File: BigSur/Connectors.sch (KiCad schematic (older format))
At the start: 32 parts, among them J1 XT30, J10 XT30, J11 Conn_01x03, J12 XT30, J13 Conn_01x04, J14 XT30, J15 XT30, J16 XT30, J2 XT30, J3 XT30, J4 XT30, J5 XT30, J6 XT30, J7 XT30, J8 XT30, J9 XT30, U4 SMD46

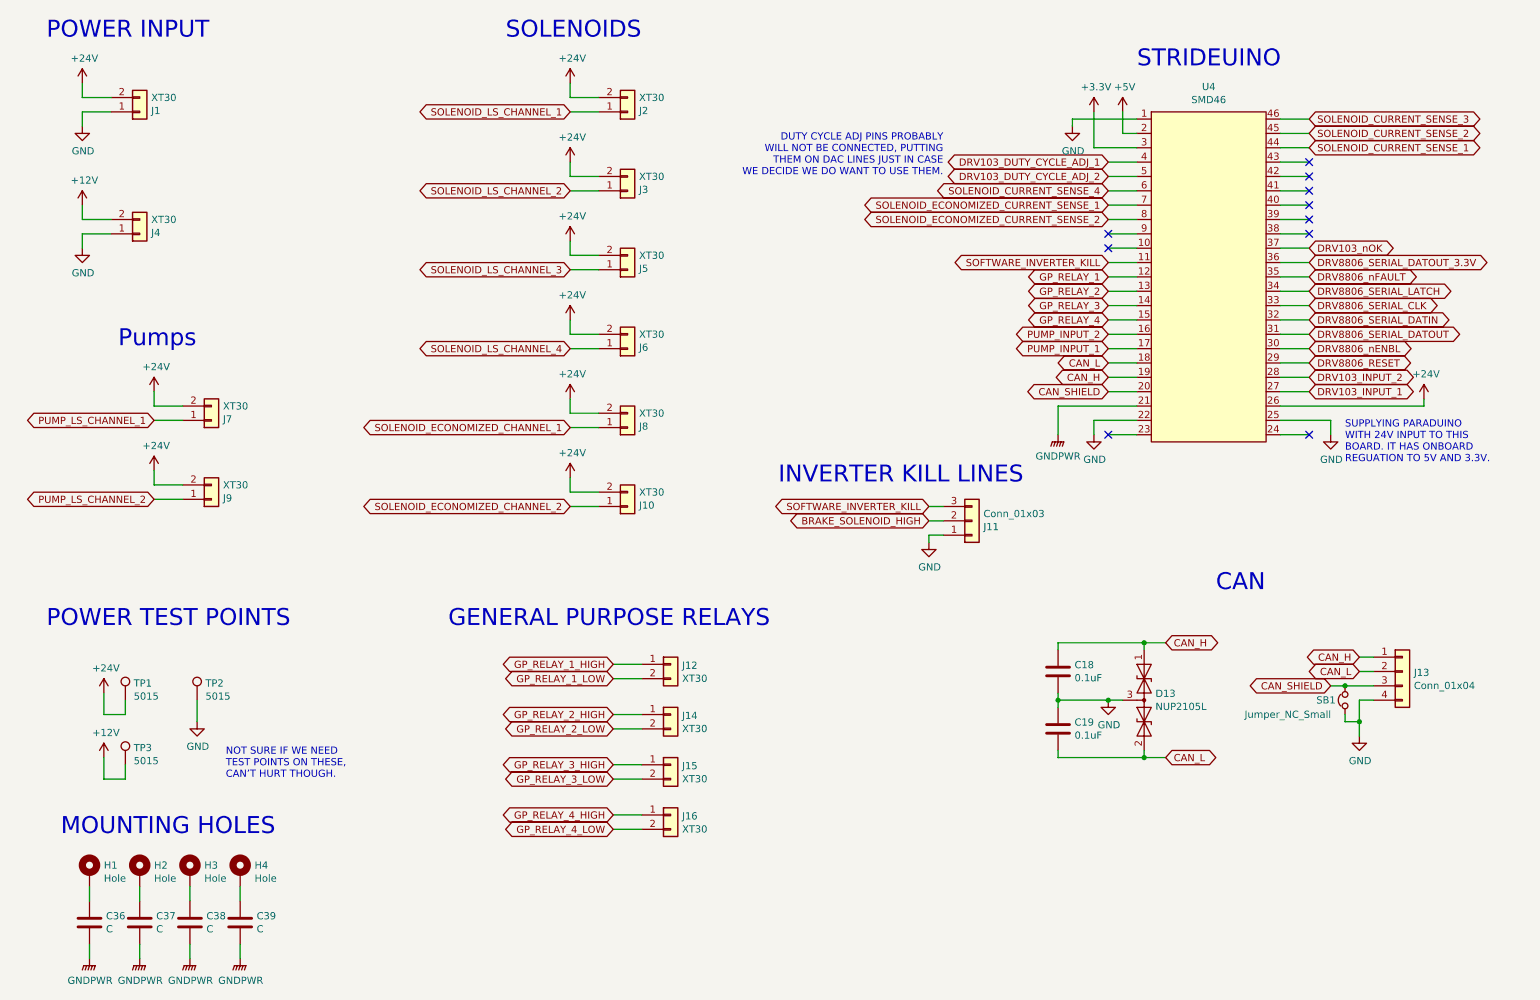
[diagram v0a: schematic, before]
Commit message: XT30 sourcing and footprints
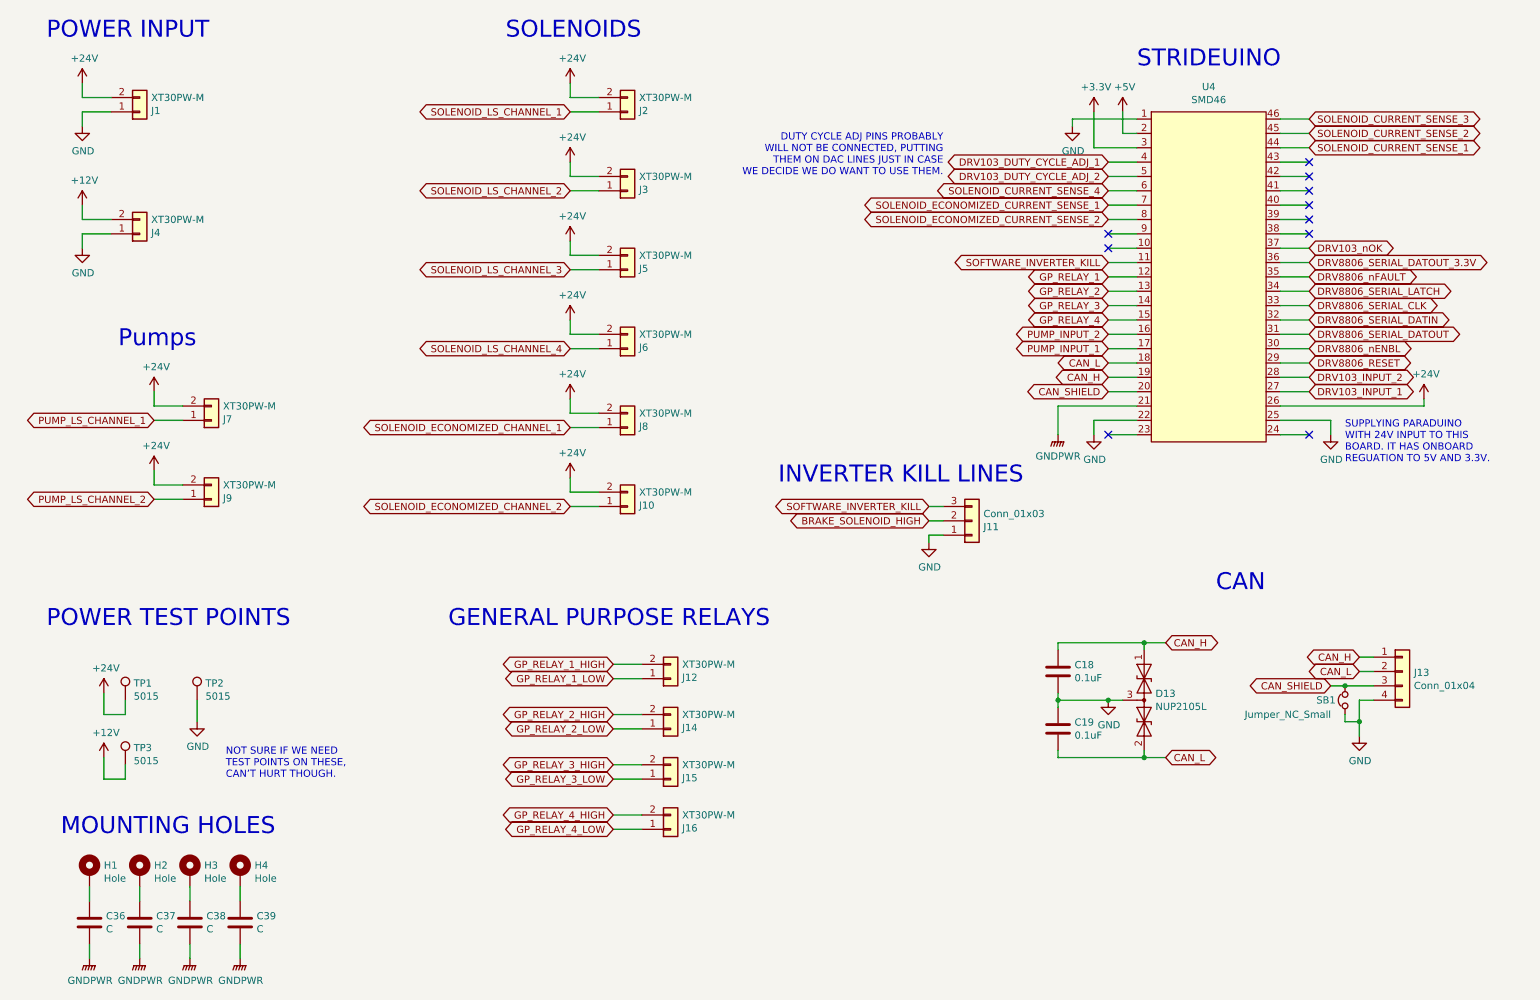
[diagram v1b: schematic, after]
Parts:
- J1, J10, J12, J14, J15, J16, J2, J3, J4, J5, J6, J7, J8, J9: value XT30 -> XT30PW-M; footprint (none) -> BigSur:AMASS_XT30PW-M; AliExpress (none) -> https://www.aliexpress.com/item/32689137918.html
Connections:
- net GP_RELAY_1_HIGH: now also J12.2 (Pin_2); no longer J12.1 (Pin_1)
- net GP_RELAY_1_LOW: now also J12.1 (Pin_1); no longer J12.2 (Pin_2)
- net GP_RELAY_2_HIGH: now also J14.2 (Pin_2); no longer J14.1 (Pin_1)
- net GP_RELAY_2_LOW: now also J14.1 (Pin_1); no longer J14.2 (Pin_2)
- net GP_RELAY_3_HIGH: now also J15.2 (Pin_2); no longer J15.1 (Pin_1)
- net GP_RELAY_3_LOW: now also J15.1 (Pin_1); no longer J15.2 (Pin_2)
- net GP_RELAY_4_HIGH: now also J16.2 (Pin_2); no longer J16.1 (Pin_1)
- net GP_RELAY_4_LOW: now also J16.1 (Pin_1); no longer J16.2 (Pin_2)

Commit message: Switched to active low brake lines
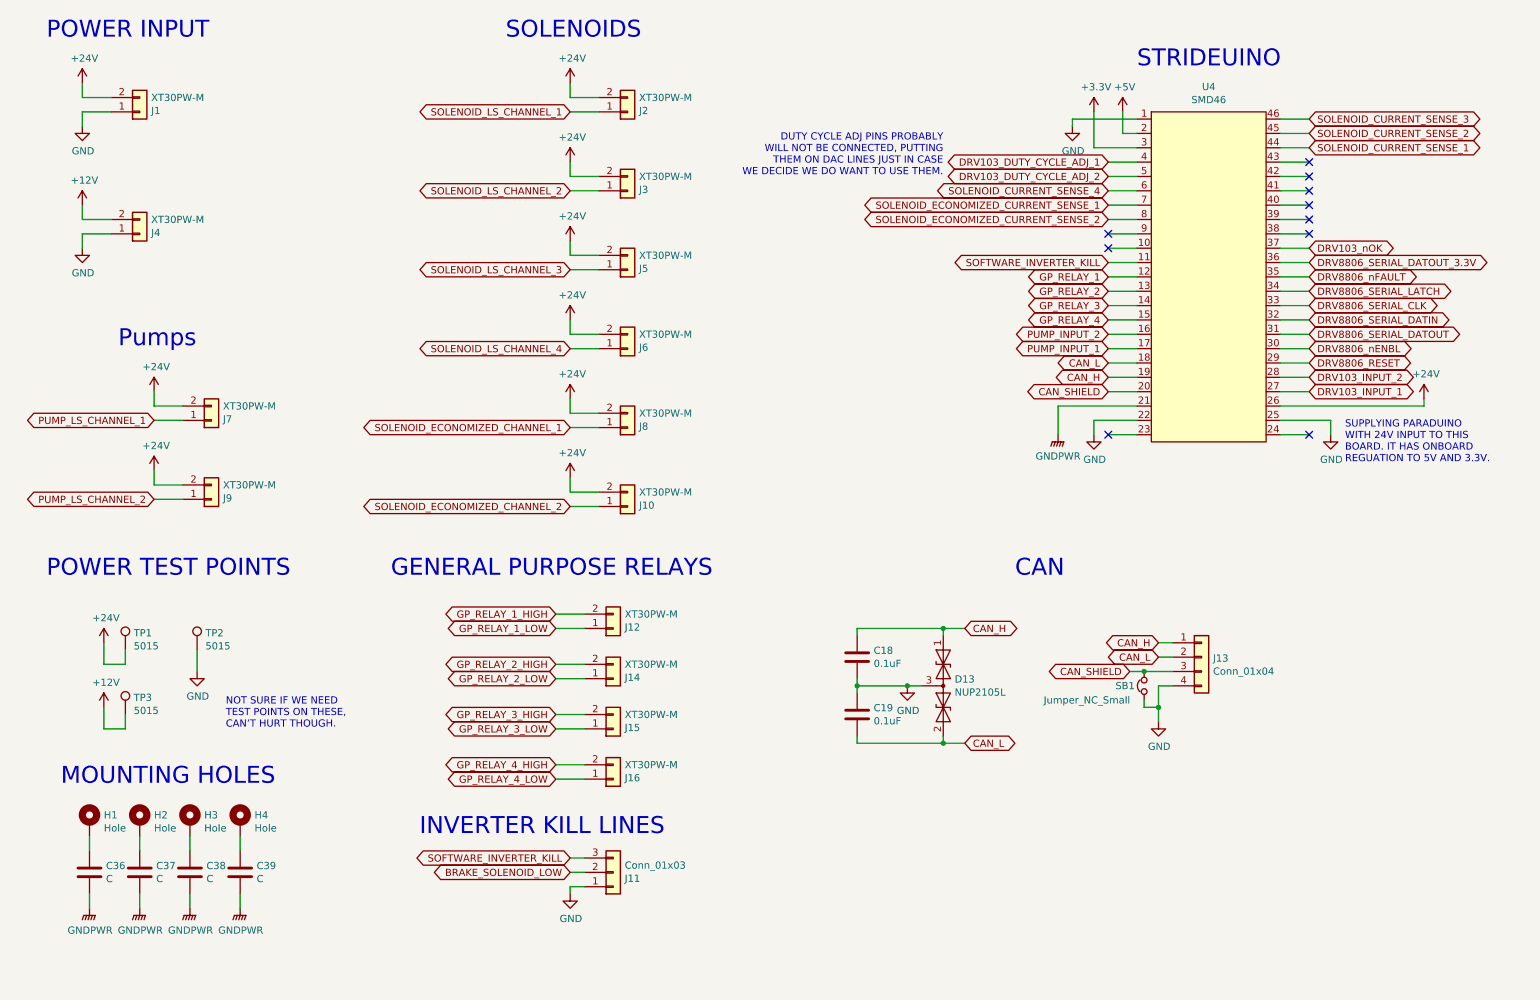
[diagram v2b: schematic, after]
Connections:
- net BRAKE_SOLENOID_HIGH renamed BRAKE_SOLENOID_LOW
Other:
- moved on the sheet: C18, C19, C36, C37, C38, C39, D13, H1, H2, H3, H4, J11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

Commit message: Initial layout pass. This will be changed many times I'm sure.
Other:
- note added: "PUMPS"
- note removed: "Pumps"
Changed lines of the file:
@@
 SOLENOID_ECONOMIZED_CHANNEL_2
 Text Notes 1350 3300 0    118  ~ 0
-Pumps
+PUMPS
 Wire Wire Line
 	1800 3700 1600 3700

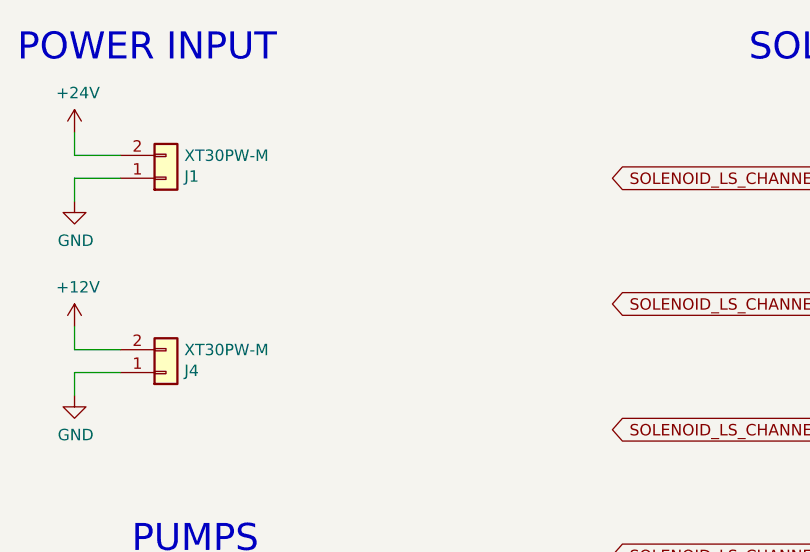
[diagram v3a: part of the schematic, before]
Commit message: Added power LEDs.
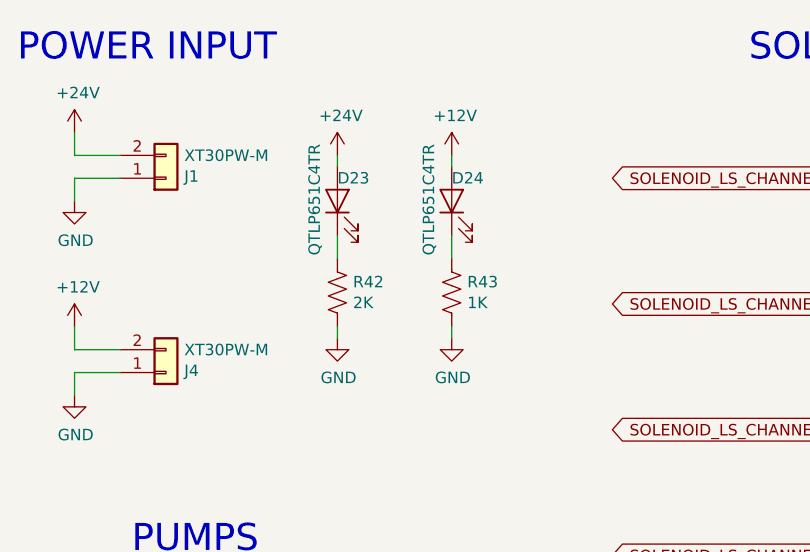
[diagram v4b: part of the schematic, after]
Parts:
- added D23, D24: QTLP651C4TR, LED_SMD:LED_1206_3216Metric_Pad1.42x1.75mm_HandSolder, symbol Device:LED
- added R42: 2K, Resistor_SMD:R_0603_1608Metric_Pad1.05x0.95mm_HandSolder, symbol Device:R_US
- added R43: 1K, Resistor_SMD:R_0603_1608Metric_Pad1.05x0.95mm_HandSolder, symbol Device:R_US
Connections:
- net +12V: now also D24.2 (A)
- net +24V: now also D23.2 (A)
- net GND: now also R42.2, R43.2
- new net: D23.1 (K), R42.1
- new net: D24.1 (K), R43.1
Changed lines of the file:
@@
 	1    0    0    1
 $EndComp
+$Comp
+L Device:LED D?
+U 1 1 5DC6BC2D
+P 2250 1750
+AR Path="/5D6EB2B2/5DC6BC2D" Ref="D?"  Part="1"
+AR Path="/5D71C3EA/5DC6BC2D" Ref="D23"  Part="1"
+F 0 "D23" V 2350 1750 50  0000 R CNN
+F 1 "QTLP651C4TR" H 2500 1850 50  0000 R CNN
+F 2 "LED_SMD:LED_1206_3216Metric_Pad1.42x1.75mm_HandSolder" H 2250 1750 50  0001 C CNN
+F 3 "https://media.digikey.com/pdf/Data%20Sheets/Everlight%20PDFs/QTLP651C-2,3,4,7,B.pdf" H 2250 1750 50  0001 C CNN
+F 4 "https://www.digikey.ca/product-detail/en/everlight-electronics-co-ltd/QTLP651C4TR/1080-1484-1-ND/7598723" V 2250 1750 50  0001 C CNN "Digikey"
+	1    2250 1750
+	0    -1   -1   0
+$EndComp
+$Comp
+L power:+24V #PWR0125
+U 1 1 5DC71029
+P 2250 1550
+AR Path="/5D71C3EA/5DC71029" Ref="#PWR0125"  Part="1"
+AR Path="/5D7D29A6/5DC71029" Ref="#PWR?"  Part="1"
+F 0 "#PWR0125" H 2250 1400 50  0001 C CNN
+F 1 "+24V" H 2265 1723 50  0000 C CNN
+F 2 "" H 2250 1550 50  0001 C CNN
+F 3 "" H 2250 1550 50  0001 C CNN
+	1    2250 1550
+	1    0    0    -1
+$EndComp
+Wire Wire Line
+	2250 1550 2250 1600
+$Comp
+L Device:R_US R42
+U 1 1 5DC76705
+P 2250 2150
+F 0 "R42" H 2318 2196 50  0000 L CNN
+F 1 "2K" H 2318 2105 50  0000 L CNN
+F 2 "Resistor_SMD:R_0603_1608Metric_Pad1.05x0.95mm_HandSolder" V 2290 2140 50  0001 C CNN
+F 3 "https://www.rohm.com/datasheet/ESR01MZPF/esr-e" H 2250 2150 50  0001 C CNN
+F 4 "ESR03EZPJ202" H 2250 2150 50  0001 C CNN "Part Number"
+F 5 "https://www.digikey.ca/product-detail/en/rohm-semiconductor/ESR03EZPJ202/RHM2.0KDCT-ND/1762928" H 2250 2150 50  0001 C CNN "Digikey"
+	1    2250 2150
+	1    0    0    -1
+$EndComp
+Wire Wire Line
+	2250 1900 2250 2000
+Wire Wire Line
+	2250 2300 2250 2350
+$Comp
+L power:GND #PWR0127
+U 1 1 5DC808D4
+P 2250 2350
+AR Path="/5D71C3EA/5DC808D4" Ref="#PWR0127"  Part="1"
+AR Path="/5D7D29A6/5DC808D4" Ref="#PWR?"  Part="1"
+F 0 "#PWR0127" H 2250 2100 50  0001 C CNN
+F 1 "GND" H 2255 2177 50  0000 C CNN
+F 2 "" H 2250 2350 50  0001 C CNN
+F 3 "" H 2250 2350 50  0001 C CNN
+	1    2250 2350
+	1    0    0    -1
+$EndComp
+$Comp
+L Device:LED D?
+U 1 1 5DC97B38
+P 2750 1750
+AR Path="/5D6EB2B2/5DC97B38" Ref="D?"  Part="1"
+AR Path="/5D71C3EA/5DC97B38" Ref="D24"  Part="1"
+F 0 "D24" V 2850 1750 50  0000 R CNN
+F 1 "QTLP651C4TR" H 3000 1850 50  0000 R CNN
+F 2 "LED_SMD:LED_1206_3216Metric_Pad1.42x1.75mm_HandSolder" H 2750 1750 50  0001 C CNN
+F 3 "https://media.digikey.com/pdf/Data%20Sheets/Everlight%20PDFs/QTLP651C-2,3,4,7,B.pdf" H 2750 1750 50  0001 C CNN
+F 4 "https://www.digikey.ca/product-detail/en/everlight-electronics-co-ltd/QTLP651C4TR/1080-1484-1-ND/7598723" V 2750 1750 50  0001 C CNN "Digikey"
+	1    2750 1750
+	0    -1   -1   0
+$EndComp
+Wire Wire Line
+	2750 1550 2750 1600
+$Comp
+L Device:R_US R43
+U 1 1 5DC97B4D
+P 2750 2150
+F 0 "R43" H 2818 2196 50  0000 L CNN
+F 1 "1K" H 2818 2105 50  0000 L CNN
+F 2 "Resistor_SMD:R_0603_1608Metric_Pad1.05x0.95mm_HandSolder" V 2790 2140 50  0001 C CNN
+F 3 "https://www.seielect.com/catalog/sei-rmcf_rmcp.pdf" H 2750 2150 50  0001 C CNN
+F 4 "https://www.digikey.ca/product-detail/en/stackpole-electronics-inc/RMCF0603JJ1K00/RMCF0603JJ1K00CT-ND/6053833" H 2750 2150 50  0001 C CNN "Digikey"
+F 5 "RMCF0603JJ1K00" H 2750 2150 50  0001 C CNN "Part Number"
+	1    2750 2150
+	1    0    0    -1
+$EndComp
+Wire Wire Line
+	2750 1900 2750 2000
+Wire Wire Line
+	2750 2300 2750 2350
+$Comp
+L power:GND #PWR0128
+U 1 1 5DC97B59
+P 2750 2350
+AR Path="/5D71C3EA/5DC97B59" Ref="#PWR0128"  Part="1"
+AR Path="/5D7D29A6/5DC97B59" Ref="#PWR?"  Part="1"
+F 0 "#PWR0128" H 2750 2100 50  0001 C CNN
+F 1 "GND" H 2755 2177 50  0000 C CNN
+F 2 "" H 2750 2350 50  0001 C CNN
+F 3 "" H 2750 2350 50  0001 C CNN
+	1    2750 2350
+	1    0    0    -1
+$EndComp
+$Comp
+L power:+12V #PWR0126
+U 1 1 5DC9E390
+P 2750 1550
+AR Path="/5D71C3EA/5DC9E390" Ref="#PWR0126"  Part="1"
+AR Path="/5D7D29A6/5DC9E390" Ref="#PWR?"  Part="1"
+F 0 "#PWR0126" H 2750 1400 50  0001 C CNN
+F 1 "+12V" H 2765 1723 50  0000 C CNN
+F 2 "" H 2750 1550 50  0001 C CNN
+F 3 "" H 2750 1550 50  0001 C CNN
+	1    2750 1550
+	1    0    0    -1
+$EndComp
 $EndSCHEMATC

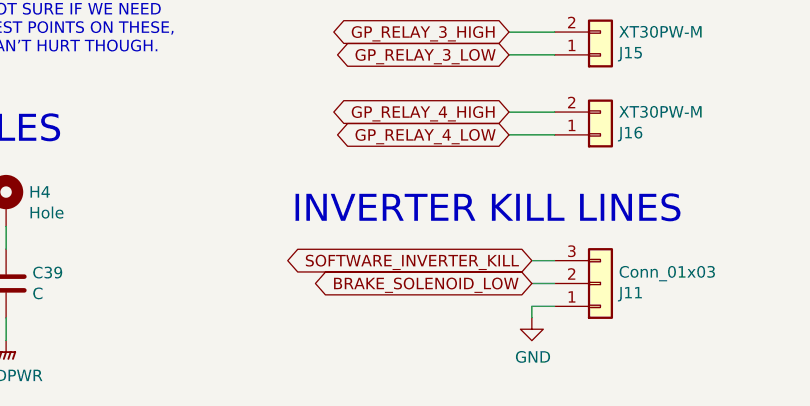
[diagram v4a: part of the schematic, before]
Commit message: Squished output connectors together, going to need to fix layout.
Also still needs CAN and inverter chill connectors.
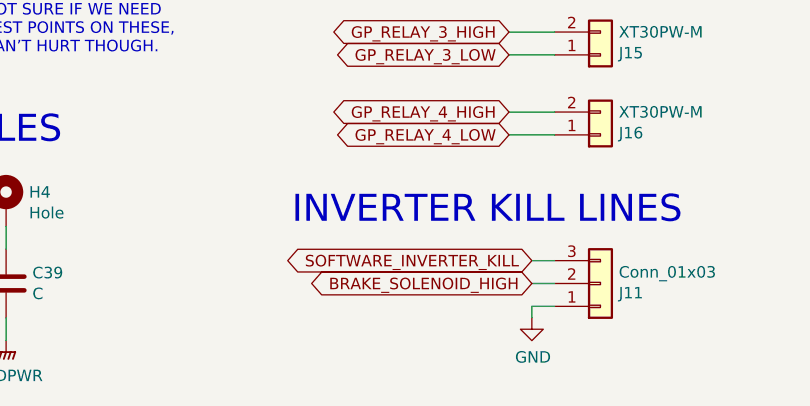
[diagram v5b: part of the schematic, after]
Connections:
- net BRAKE_SOLENOID_LOW renamed BRAKE_SOLENOID_HIGH
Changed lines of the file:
@@
 EESchema Schematic File Version 4
 LIBS:BigSur-cache
-EELAYER 30 0
+EELAYER 29 0
 EELAYER END
 $Descr A4 11693 8268
@@
 	4600 6950 4500 6950
 Text GLabel 4500 6950 0    50   BiDi ~ 0
-BRAKE_SOLENOID_LOW
+BRAKE_SOLENOID_HIGH
 Wire Wire Line
 	4600 7050 4500 7050

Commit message: Finished another layout pass.
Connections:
- net DRV8806_SERIAL_DATOUT is gone; now on net DRV8806_SERIAL_DATOUT_3.3V: U4.31
- net DRV8806_SERIAL_DATOUT_3.3V: no longer U4.36
- no-connect marks 10 -> 11
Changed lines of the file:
@@
 Wire Wire Line
 	9650 3200 9450 3200
-Text GLabel 9650 3200 2    50   BiDi ~ 0
-DRV8806_SERIAL_DATOUT
 Wire Wire Line
 	9650 3300 9450 3300
@@
 Text GLabel 9650 2800 2    50   BiDi ~ 0
 DRV8806_nFAULT
-Text GLabel 9650 2700 2    50   BiDi ~ 0
+Text GLabel 9650 3200 2    50   BiDi ~ 0
 DRV8806_SERIAL_DATOUT_3.3V
 Text GLabel 9650 2600 2    50   BiDi ~ 0
@@
 	1    0    0    -1
 $EndComp
+NoConn ~ 9650 2700
 $EndSCHEMATC
